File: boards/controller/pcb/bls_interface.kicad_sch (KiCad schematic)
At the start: 8 parts, among them J11001 Power, J11002 SPI, J11003 PWM

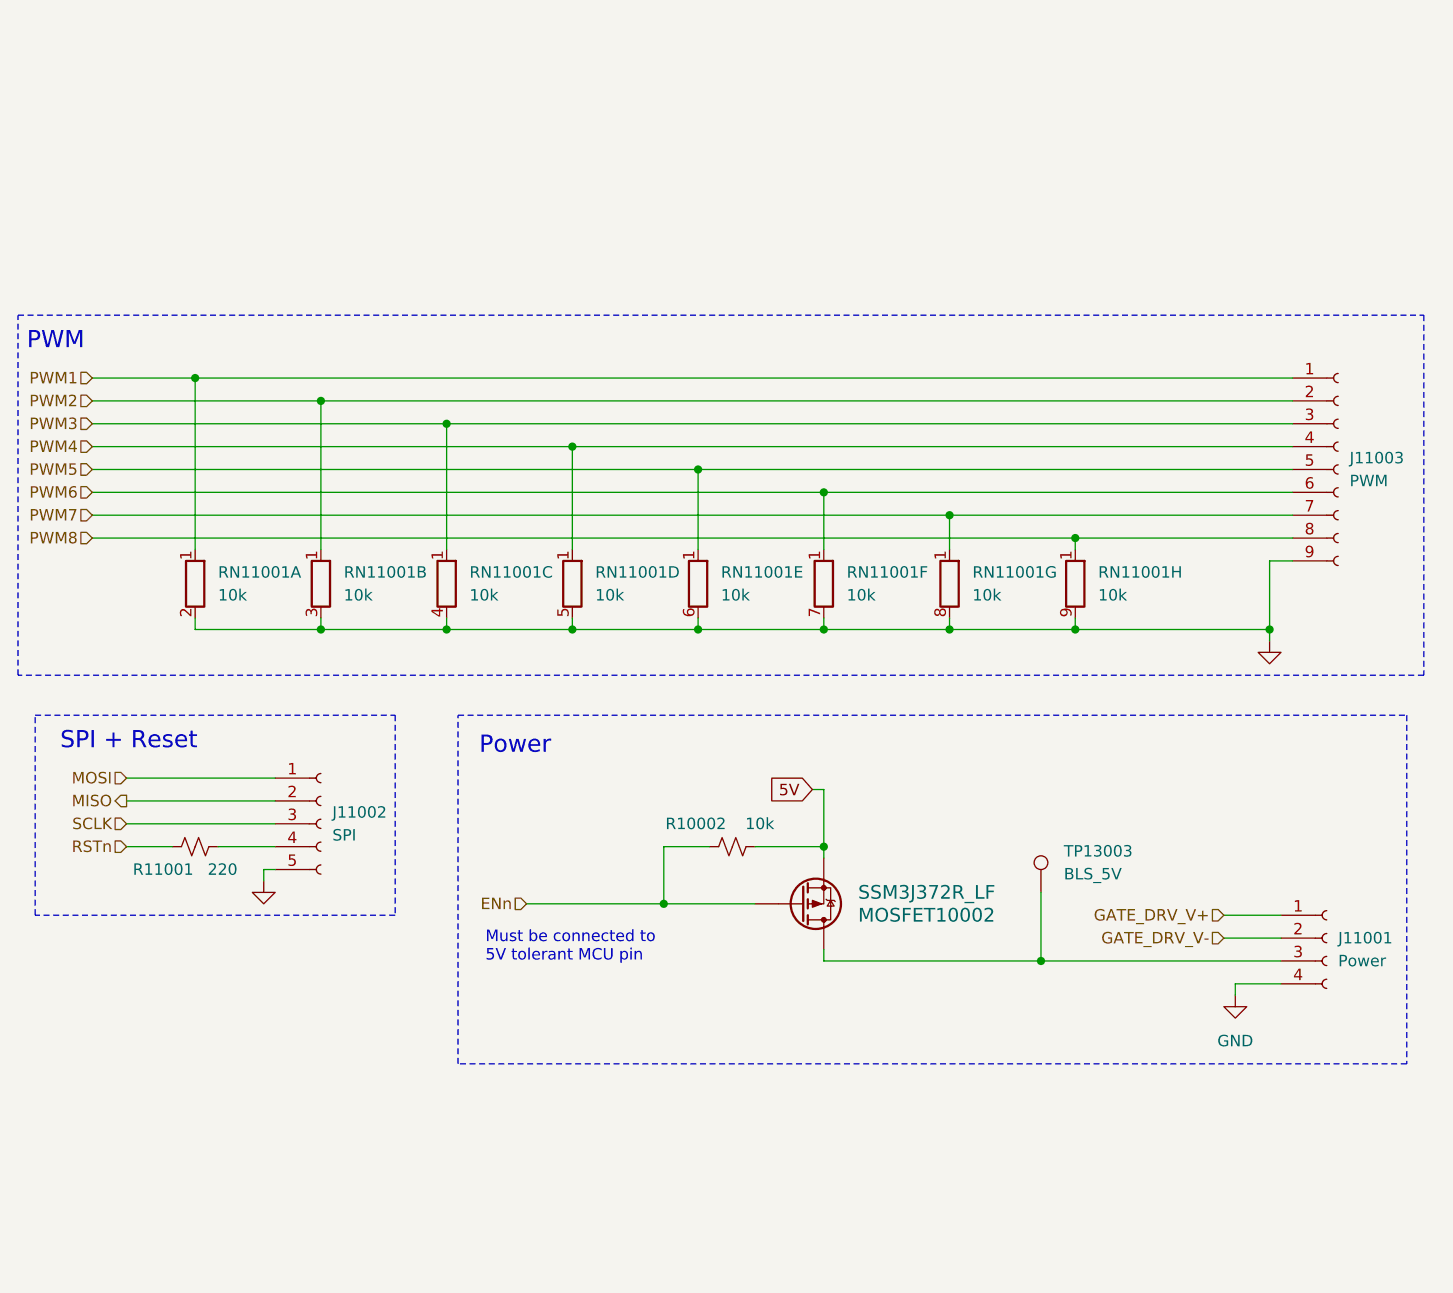
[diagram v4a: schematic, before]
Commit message: controller: pcb: Update schematic + layout
Signed-off-by: Nicholas Loehrke <nicholasnloehrke@gmail.com>
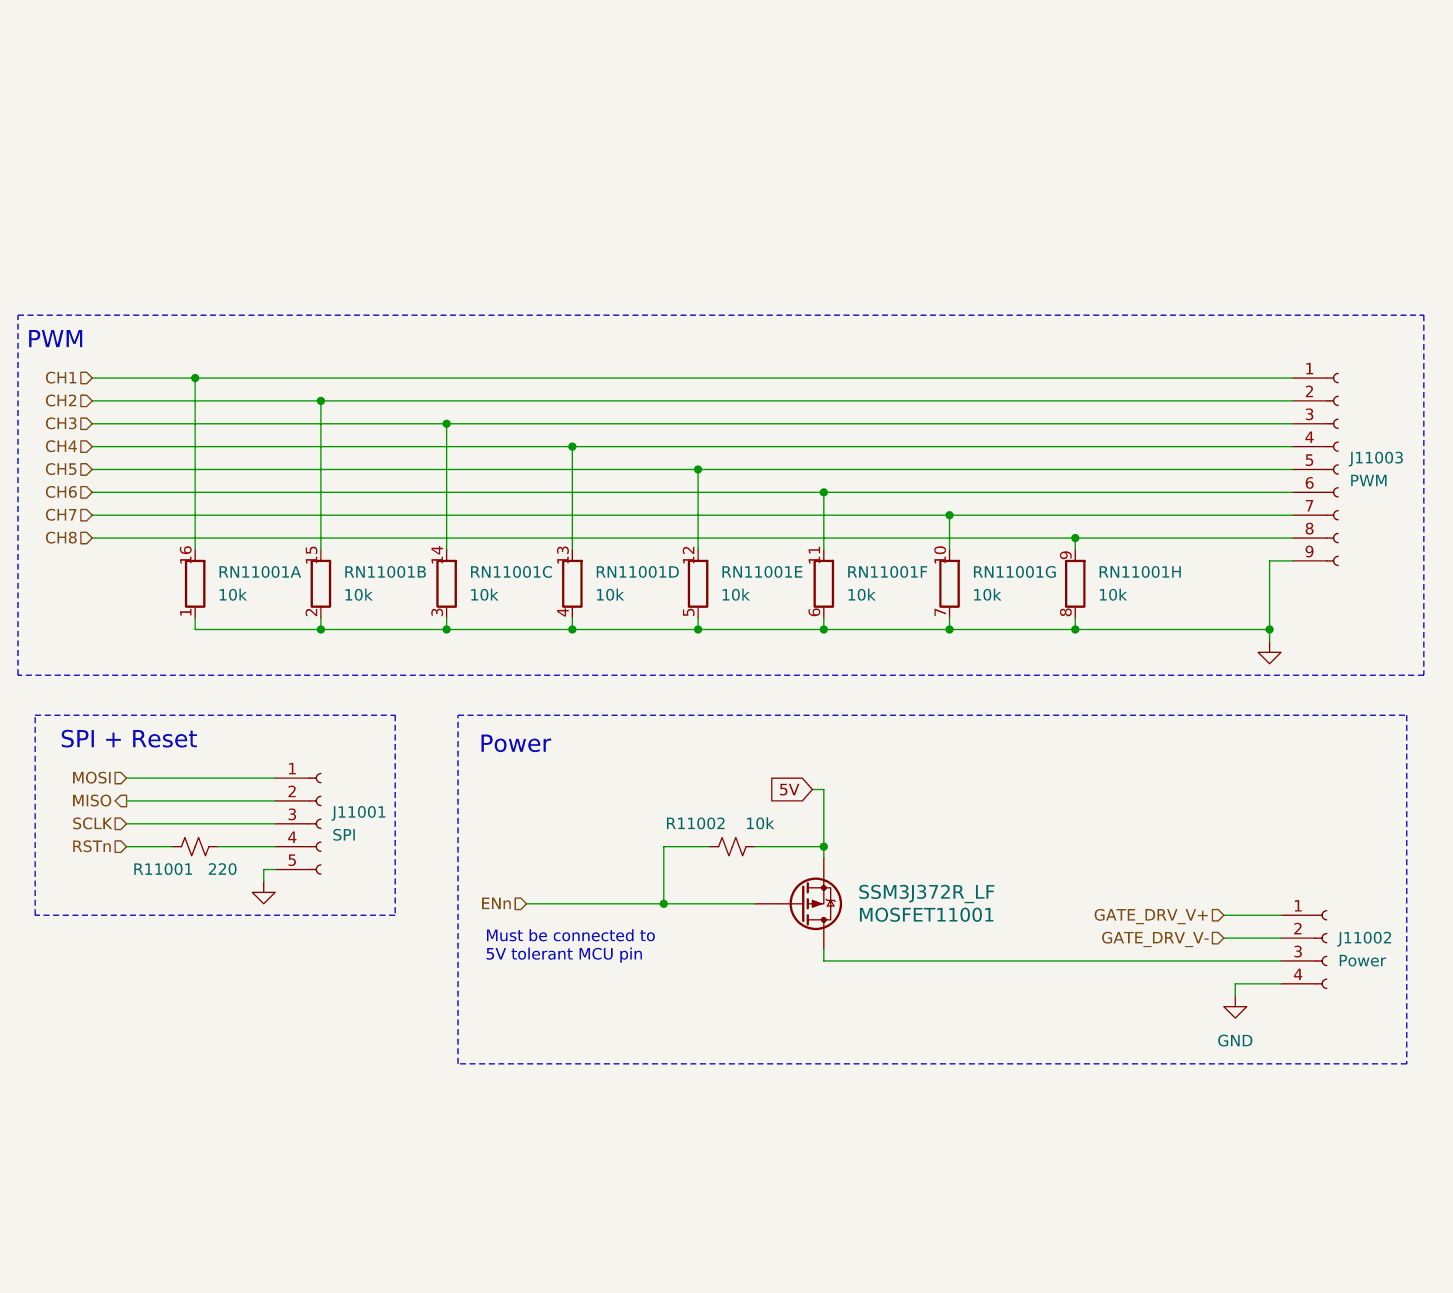
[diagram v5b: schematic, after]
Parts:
- removed RN11001: 10k, Resistor_THT:R_Array_SIP9, symbol Device:R_Network08_Split
- removed TP13003: BLS_5V, symbol Connector:TestPoint
- added RN11001: 10k, YC248-JR-0710KL:YC248-JR-0710KL, symbol Device:R_Pack08_Split
- MOSFET11001: renamed from MOSFET10002; footprint SOT-23F_TOS -> SSM3J372R_LF:SSM3J372R_LF
- R11001: footprint (none) -> Resistor_SMD:R_0603_1608Metric
- R11002: renamed from R10002; footprint (none) -> Resistor_SMD:R_0402_1005Metric
- renumbered J11002 to J11001, J11001 to J11002
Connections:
- net GND: now also RN11001.1 (R1.1), RN11001.2 (R2.1), RN11001.3 (R3.1), RN11001.4 (R4.1), RN11001.5 (R5.1), RN11001.6 (R6.1), RN11001.7 (R7.1), RN11001.8 (R8.1)
- net PWM1 renamed CH1
- net CH1: now also RN11001.16 (R1.2)
- net PWM2 renamed CH2
- net CH2: now also RN11001.15 (R2.2)
- net PWM3 renamed CH3
- net CH3: now also RN11001.14 (R3.2)
- net PWM4 renamed CH4
- net CH4: now also RN11001.13 (R4.2)
- net PWM5 renamed CH5
- net CH5: now also RN11001.12 (R5.2)
- net PWM6 renamed CH6
- net CH6: now also RN11001.11 (R6.2)
- net PWM7 renamed CH7
- net CH7: now also RN11001.10 (R7.2)
- net PWM8 renamed CH8
- net CH8: now also RN11001.9 (R8.2)

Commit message: controller: Update BOM
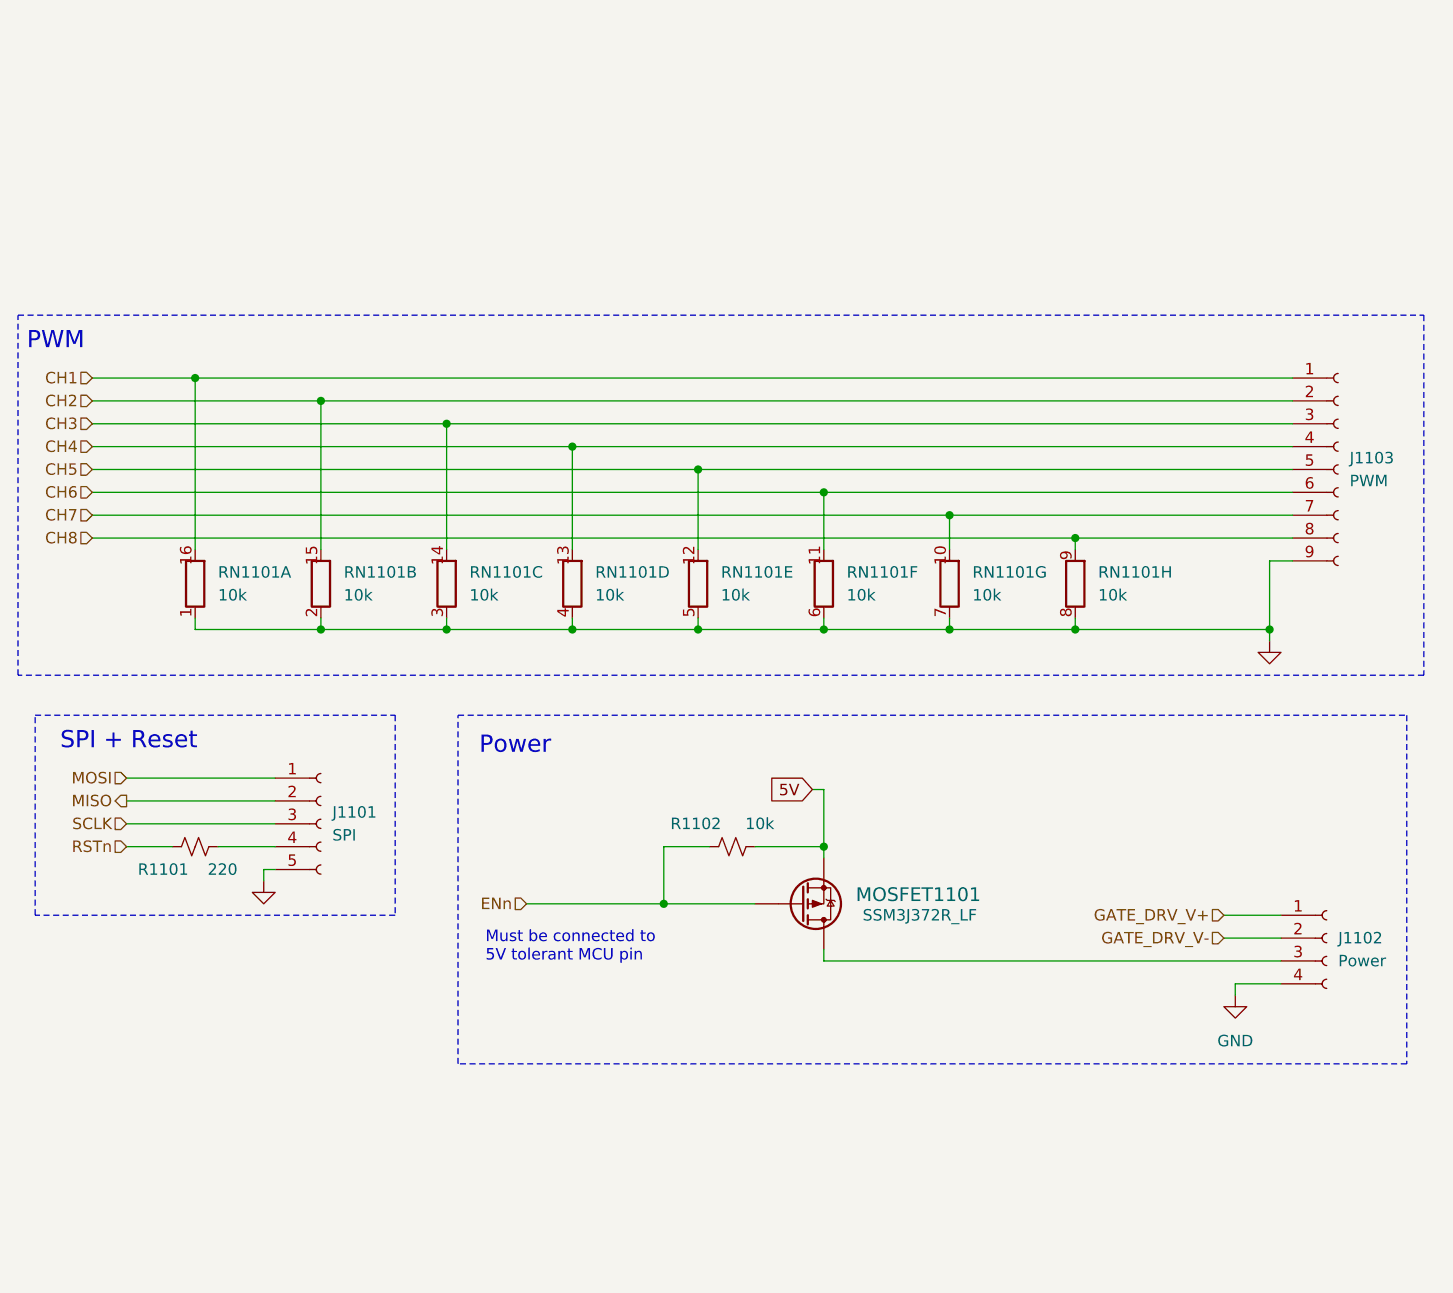
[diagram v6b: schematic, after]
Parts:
- MOSFET1101: renamed from MOSFET11001; MPN (none) -> SSM3J372R_LF
- R1101: renamed from R11001; footprint Resistor_SMD:R_0603_1608Metric -> Resistor_SMD:R_0402_1005Metric
- RN1101: renamed from RN11001; MPN (none) -> YC248-JR-0710KL
- renumbered J11001 to J1101, J11002 to J1102, J11003 to J1103, R11002 to R1102
